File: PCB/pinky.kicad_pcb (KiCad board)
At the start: 2 copper layers, 120.5 x 85.5 mm, 47 parts, among them SW10 SW_Kailh_Choc_PG1350, SW11 SW_Kailh_Choc_PG1350, SW12 SW_Kailh_Choc_PG1350, SW13 SW_Kailh_Choc_PG1350, SW14 SW_Kailh_Choc_PG1350, SW15 SW_Kailh_Choc_PG1350, SW16 SW_Kailh_Choc_PG1350, SW17 SW_Kailh_Choc_PG1350, SW18 SW_Kailh_Choc_PG1350, SW2 SW_Kailh_Choc_PG1350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

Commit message: Updates pull
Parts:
- removed RESET: SW_Push, Pinky:ResetSW
- removed SW_PWR: SW_SPDT_321, Pinky:MSK12C02
- added RESET19: ResetSW, Pinky:ResetSW, F.Cu at (95.3, 65.0)
- added SW_PWR1: MSK12C02, Pinky:MSK12C02, F.Cu at (91.3, 71.4)
- BT1: value Battery_Cell -> JST_PH
- D1, D10, D11, D12, D13, D14, D15, D16, D17, D2, D3, D4, D5, D6, D7, D8, D9: value D -> D_SOD123
- JP1, JP2, JP3, JP4: value SDA -> Jumper
- SW10, SW11, SW12, SW13, SW14, SW15, SW16, SW17, SW18, SW2, SW3, SW4, SW5, SW6, SW7, SW8, SW9: value SW_Kailh_Choc_PG1350 -> Switch
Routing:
- net +BATT: track 8.78 -> 0.00 mm, vias 1 -> 0
- net Net-(SW_PWR1-B): track 90.8 -> 85.1 mm, vias 2 -> 1
- net unconnected-(SW1-C-Pad1): track 2.57 -> 0.00 mm
- net unconnected-(SW1-C-Pad1)_1: track 2.55 -> 0.00 mm
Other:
- board text removed: "PWR"

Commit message: Added a "decoder" of the currently active side for the power switch and cleaned up a clutter net
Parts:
- added JP10: Jumper, Pinky:Jumper, F.Cu at (55.3, 86.4)
- added JP5: Jumper, Pinky:Jumper, B.Cu at (55.3, 81.3)
- added JP6: Jumper, Pinky:Jumper, F.Cu at (55.3, 81.3)
- added JP7: Jumper, Pinky:Jumper, B.Cu at (55.3, 83.9)
- added JP8: Jumper, Pinky:Jumper, F.Cu at (55.3, 83.9)
- added JP9: Jumper, Pinky:Jumper, B.Cu at (55.3, 86.4)
- U1: moved to B.Cu
- moved RESET19 49.2 mm to (46.1, 64.0)
- moved U1 43.5 mm to (54.9, 90.8), turned to 180 degrees
- moved SW_PWR1 24.9 mm to (68.2, 62.4), turned to -90 degrees
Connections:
- U1 pad 14: GND -> Net-(JP6-Pad2)
- U1 pad 15: RESET -> Net-(U1-RESET)
- U1 pad 16: +BATT -> Net-(U1-EXT_VCC)
- U1 pad 2: unconnected-(U1-D0/P0.08-Pad2) -> Net-(U1-D0/P0.08)
- U1 pad 3: unconnected-(U1-GND-Pad3) -> Net-(JP7-Pad2)
- U1 pad 4: unconnected-(U1-GND-Pad4) -> Net-(JP9-Pad2)
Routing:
- net +BATT: track 0.00 -> 17.2 mm, vias 0 -> 2
- net GND: track 0.00 -> 11.9 mm, vias 0 -> 1
- net unconnected-(SW_PWR1-C-Pad1): track 0.00 -> 7.56 mm, vias 0 -> 1
- net Net-(JP6-Pad2): track 0.00 -> 7.14 mm
- net Net-(U1-EXT_VCC): track 0.00 -> 7.13 mm
- net Net-(U1-RESET): track 0.00 -> 7.13 mm
- net Net-(JP7-Pad2): track 0.00 -> 6.79 mm
- net Net-(JP9-Pad2): track 0.00 -> 6.79 mm
- net Net-(U1-D0/P0.08): track 0.00 -> 6.78 mm
- net RESET: track 8.19 -> 11.9 mm, vias 0 -> 1
- net Net-(SW_PWR1-B): track 85.1 -> 87.6 mm, vias 1 -> 2

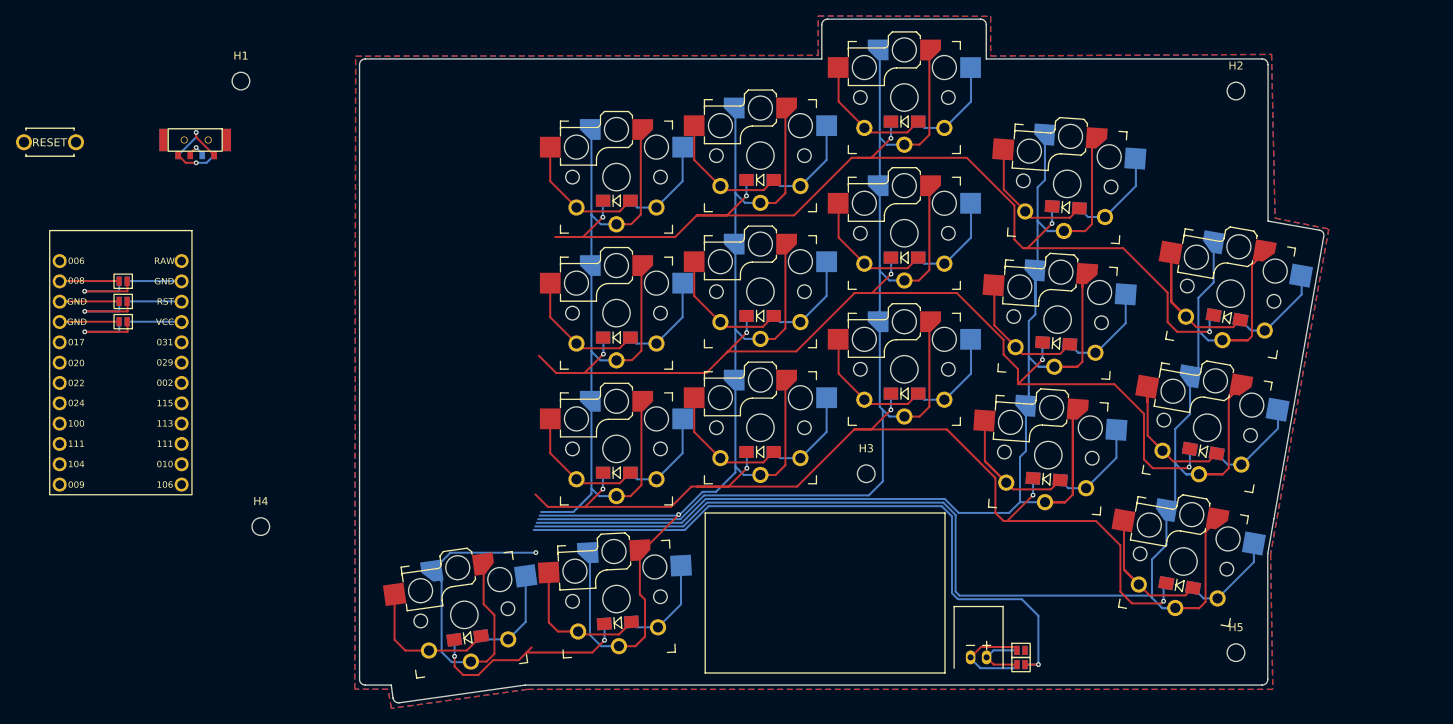
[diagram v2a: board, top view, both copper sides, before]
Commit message: Shaping up the layout of the footprints
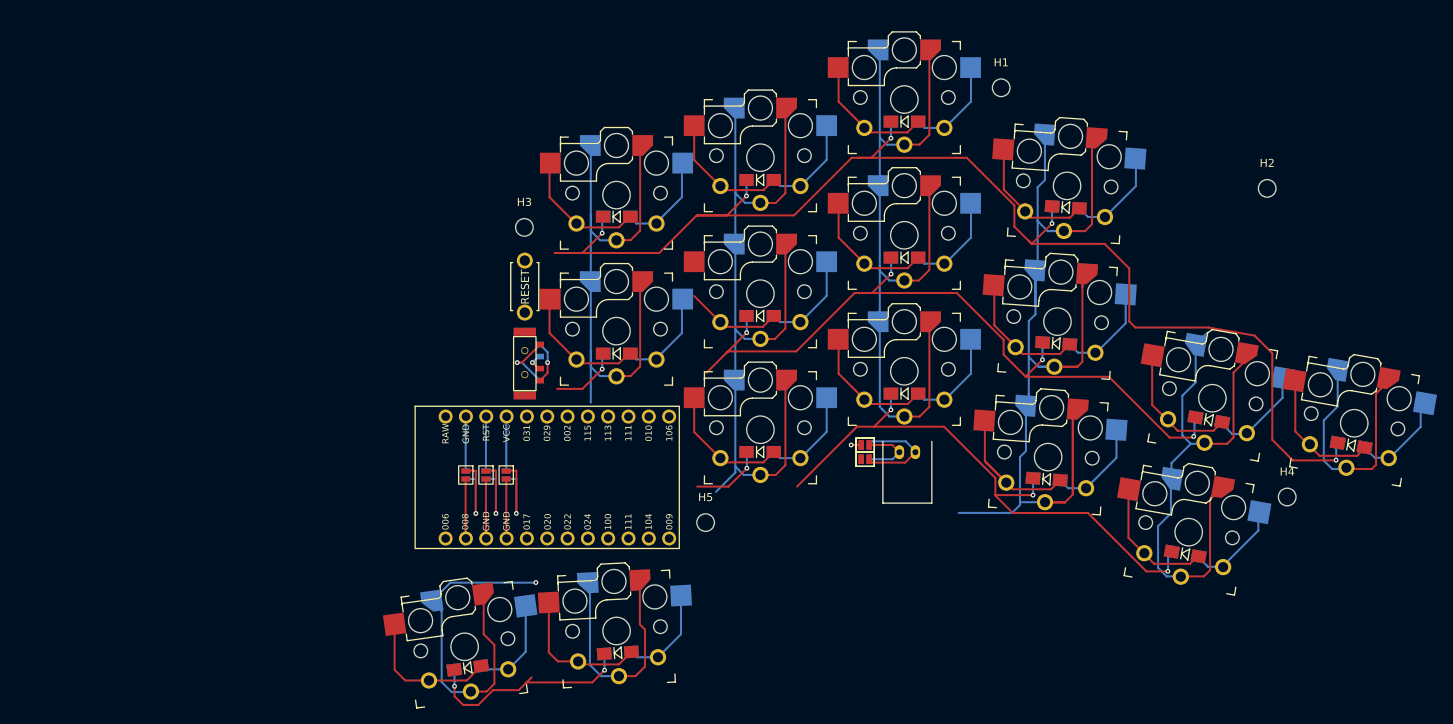
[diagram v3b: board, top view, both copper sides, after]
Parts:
- removed D3: D_SOD123, Pinky:D_SOD123
- removed the JP1 at (167.5, 127.5)
- removed the JP2 at (167.5, 129.2)
- removed the JP3 at (167.5, 129.2)
- removed the JP4 at (167.5, 127.5)
- removed SW4: Switch, Pinky:Switch
- added JP1: SDA, Pinky:Jumper, B.Cu at (148.0, 103.6)
- added JP1: Jumper, Pinky:Jumper, B.Cu at (148.0, 103.6)
- added JP2: SDA, Pinky:Jumper, F.Cu at (148.0, 101.8)
- added JP2: Jumper, Pinky:Jumper, F.Cu at (148.0, 101.8)
- added JP3: SDA, Pinky:Jumper, B.Cu at (148.0, 101.8)
- added JP3: Jumper, Pinky:Jumper, B.Cu at (148.0, 101.8)
- added JP4: SDA, Pinky:Jumper, F.Cu at (148.0, 103.6)
- added JP4: Jumper, Pinky:Jumper, F.Cu at (148.0, 103.6)
- D1, D10, D11, D12, D13, D14, D15, D16, D17, D2, D4, D5, D6, D7, D8, D9: value D_SOD123 -> D
- RESET19: value ResetSW -> Val**
- SW10, SW11, SW12, SW13, SW14, SW15, SW16, SW17, SW18, SW2, SW3, SW5, SW6, SW7, SW8, SW9: value Switch -> SW_Kailh_Choc_PG1350
- moved H4 128.4 mm to (200.8, 108.3)
- moved H1 95.0 mm to (165.1, 57.1)
- moved H5 68.3 mm to (128.1, 111.5)
- moved RESET19 62.0 mm to (105.5, 82.0), turned to 90 degrees
- moved U1 54.8 mm to (107.6, 105.9), turned to -90 degrees
- moved H3 52.7 mm to (105.5, 74.6)
- moved JP10 51.6 mm to (103.2, 105.5), turned to -90 degrees
- moved JP9 51.6 mm to (103.2, 105.5), turned to 90 degrees
- moved JP7 50.3 mm to (100.6, 105.5), turned to 90 degrees
- moved JP8 50.3 mm to (100.6, 105.5), turned to -90 degrees
- moved JP5 49.2 mm to (98.1, 105.5), turned to 90 degrees
- moved JP6 49.2 mm to (98.1, 105.5), turned to -90 degrees
- moved SW_PWR1 44.1 mm to (104.2, 87.8), turned to 0 degrees
- moved BT1 27.9 mm to (152.3, 102.7), turned to 0 degrees
- moved D15 22.2 mm to (208.8, 101.8)
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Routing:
- net col_E: track 211.6 -> 99.4 mm
- net Net-(SW_PWR1-B): track 87.6 -> 4.61 mm
- net col_D: track 200.5 -> 146.1 mm
- net col_C: track 151.4 -> 97.4 mm
- net row_C: track 128.8 -> 81.1 mm, vias 5 -> 4
- net col_A: track 148.8 -> 114.9 mm
- net col_B: track 159.8 -> 130.3 mm, vias 1 -> 0
- net row_A: track 131.6 -> 159.9 mm
- net Net-(D3-A): track 28.2 -> 0.00 mm
- net row_B: track 129.6 -> 102.7 mm
- net Net-(D15-A): track 37.8 -> 28.2 mm
- net unconnected-(SW_PWR1-C-Pad1): track 0.00 -> 7.56 mm, vias 0 -> 1
- net unconnected-(SW_PWR1-C-Pad1)_1: track 7.56 -> 0.00 mm, vias 1 -> 0
- net Net-(D6-A): track 28.1 -> 23.8 mm
- net Net-(D16-A): track 32.1 -> 29.1 mm
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- removed copper zone on B.Cu, net GND
- removed copper zone on F.Cu, net GND
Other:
- board outline removed

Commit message: Footprint updates pull
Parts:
- removed the JP1 at (148.0, 103.6) (x2)
- removed the JP2 at (148.0, 101.8) (x2)
- removed the JP3 at (148.0, 101.8) (x2)
- removed the JP4 at (148.0, 103.6) (x2)
- added JP1: SDA, Pinky:Jumper, B.Cu at (148.0, 103.6)
- added JP1: Jumper, Pinky:Jumper, B.Cu at (148.0, 103.6)
- added JP2: SDA, Pinky:Jumper, F.Cu at (148.0, 101.8)
- added JP2: Jumper, Pinky:Jumper, F.Cu at (148.0, 101.8)
- added JP3: SDA, Pinky:Jumper, B.Cu at (148.0, 101.8)
- added JP3: Jumper, Pinky:Jumper, B.Cu at (148.0, 101.8)
- added JP4: SDA, Pinky:Jumper, F.Cu at (148.0, 103.6)
- added JP4: Jumper, Pinky:Jumper, F.Cu at (148.0, 103.6)
- D1, D10, D11, D12, D13, D14, D15, D16, D17, D2, D4, D5, D6, D7, D8, D9: value D -> D_SOD123
- RESET19: value Val** -> ResetSW
- SW10, SW11, SW12, SW13, SW14, SW15, SW16, SW17, SW18, SW2, SW3, SW5, SW6, SW7, SW8, SW9: value SW_Kailh_Choc_PG1350 -> Switch
